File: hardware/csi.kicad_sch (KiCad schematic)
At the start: 1 part, among them J5 Conn_01x22_Female

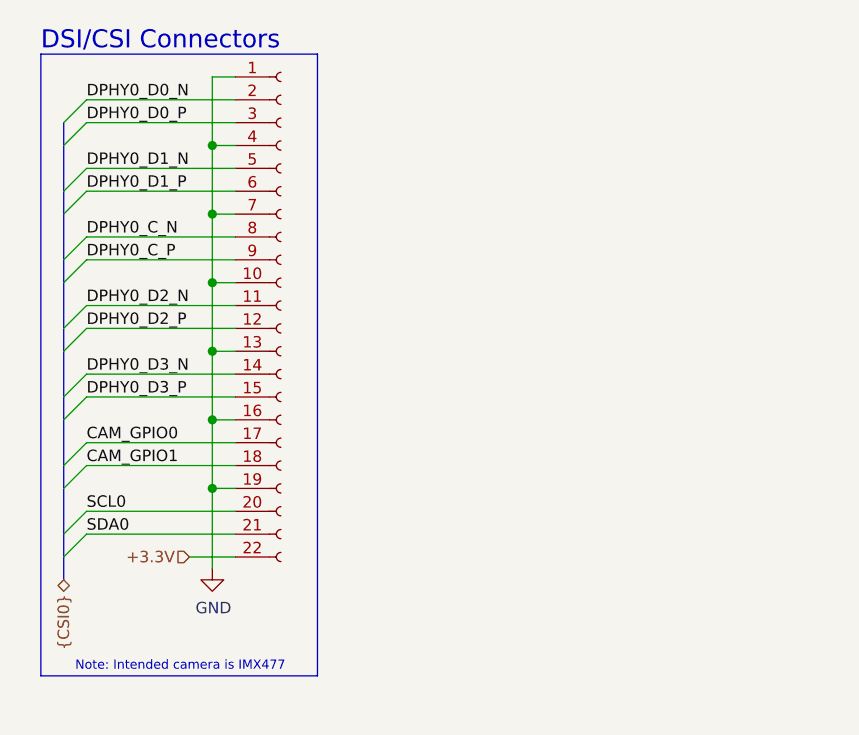
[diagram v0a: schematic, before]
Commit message: Add second camera, magnet load switch and schematic fixes
- Second camera J11 on MIPI1: I2C on ID_SD/ID_SC with 2.2k pull-ups,
  power enable on GPIO14/15 (CAM1_GPIO0/1); both cameras take 3.3 V
  from CM5_3.3V
- Magnet power switch: IC9 output is now +5V_AON, TPS22965 load switch
  IC15 drives +5V, J12 carries +5V_AON / MAG_ON / GND with R29
  pull-down; new TPS22965 symbol library
- Power: 4 A TPSM53604, 8 mOhm input sense resistor, C39/C40 bulk caps,
  F1-F3 battery polyfuses; 5 V raised to 5.115 V (R24 2.43k, 0.5 %
  feedback resistors); 47 uF at the CM5 5 V pins
- BMI270 on SPI and WSEN-PADS on I2C in serial_peripherals.kicad_sch
- Breakout headers J9/J13 with 5 V, 3.3 V and GND
- References renamed U -> IC; net classes for DPHY1, +5V, +5V_AON, +3.3V
- ERC clean (0 errors, 0 warnings); PCB update from the schematic is
  still in progress

Co-Authored-By: Claude Opus 5.5 <noreply@anthropic.com>
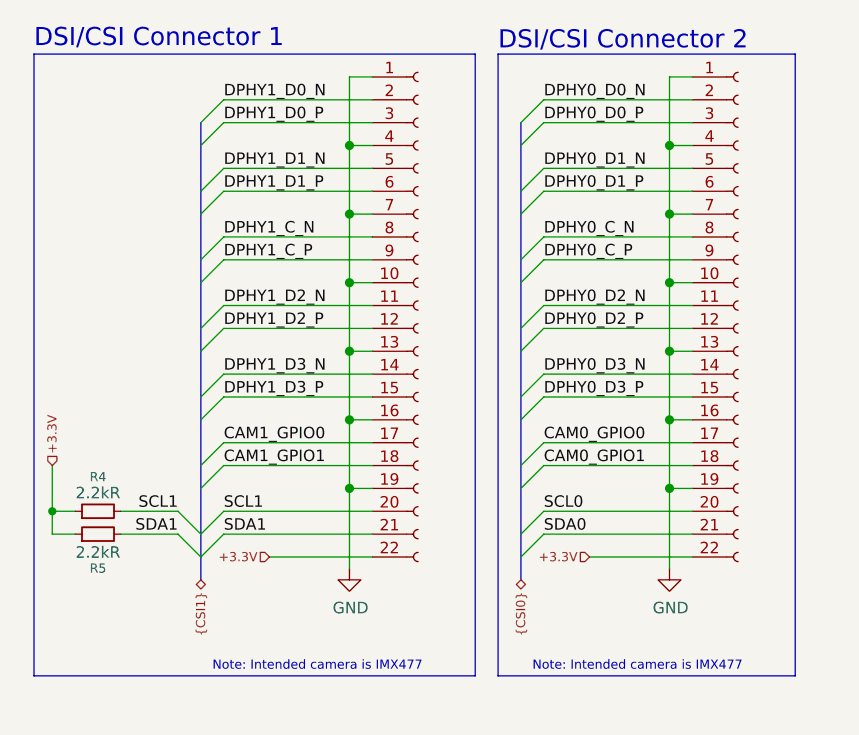
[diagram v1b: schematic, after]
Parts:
- added J11: Conn_01x22_Female, CM5IO:Hirose_FH12-22S-0.5SH_1x22-1MP_P0.50mm_Horizontal, symbol Connector:Conn_01x22_Socket
- added R4, R5: 2.2kR, Resistor_SMD:R_0402_1005Metric, symbol Device:R_Small
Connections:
- net +3.3V: now also J11.22 (Pin_22), R4.1, R5.1
- net GND: now also J11.1 (Pin_1), J11.10 (Pin_10), J11.13 (Pin_13), J11.16 (Pin_16), J11.19 (Pin_19), J11.4 (Pin_4), J11.7 (Pin_7)
- net CAM_GPIO0 renamed CAM0_GPIO0
- net CAM_GPIO1 renamed CAM0_GPIO1
- new net CAM1_GPIO0: J11.17 (Pin_17)
- new net CAM1_GPIO1: J11.18 (Pin_18)
- new net DPHY1_C_N: J11.8 (Pin_8)
- new net DPHY1_C_P: J11.9 (Pin_9)
- new net DPHY1_D0_N: J11.2 (Pin_2)
- new net DPHY1_D0_P: J11.3 (Pin_3)
- new net DPHY1_D1_N: J11.5 (Pin_5)
- new net DPHY1_D1_P: J11.6 (Pin_6)
- new net DPHY1_D2_N: J11.11 (Pin_11)
- new net DPHY1_D2_P: J11.12 (Pin_12)
- new net DPHY1_D3_N: J11.14 (Pin_14)
- new net DPHY1_D3_P: J11.15 (Pin_15)
- new net SCL1: J11.20 (Pin_20), R4.2
- new net SDA1: J11.21 (Pin_21), R5.2
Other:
- note added: "DSI/CSI Connector 1"
- note added: "DSI/CSI Connector 2"
- note removed: "DSI/CSI Connectors"

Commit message: Add switchable ESC power, vertical camera connectors and 3.3 V decoupling
- ESC power switch on the root sheet:
  - Battery input J6 changes to XT60PW-M. New XT60PW-F J14 carries switched
    power to both ESCs.
  - Q3 (onsemi NTMFS5C404NLT1G, 40 V, 0.67 mOhm) is driven by the photovoltaic
    driver IC16 (Vishay VOM1271T) from RP2354A GPIO14 (ESC_PWR_EN) via R31.
  - Soft start C46/D6/R32 keeps Q3 in its SOA while the ESC capacitors charge.
    D7 clamps the gate when the battery is unplugged or the thrusters windmill.
  - Static switch with no current limit: the battery BMS protects. Firmware
    timing rules are in the schematic note and the README.
- Camera connectors J5/J11 are now Molex 501951-2230 (vertical, flip lock).
  The footprint numbers pads n = Molex circuit 23-n so a standard Pi 22-pin
  cable lands GND on pin 1, as on the CM5 IO Board.
- Decoupling: 10 uF + 100 nF at the CM5 3.3 V output, 10 uF at each camera
  supply pin.
- Polyfuses F1-F3 removed; the battery feeds the charger path directly.
- New libraries VOM1271T, NTMFS5C404NL, Molex and Vishay, with 3D models.
- PCB updated from the schematic. The layout will be redone.

Co-Authored-By: Claude Opus 5.5 <noreply@anthropic.com>
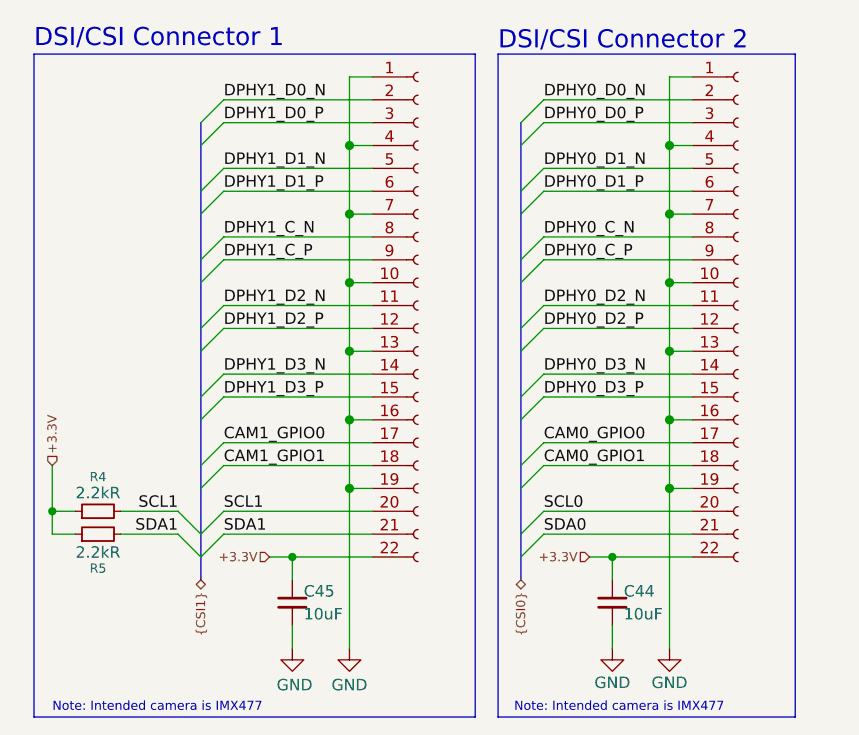
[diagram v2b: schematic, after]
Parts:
- added C44, C45: 10uF, Capacitor_SMD:C_0603_1608Metric, symbol Device:C_Small
- J11, J5: footprint CM5IO:Hirose_FH12-22S-0.5SH_1x22-1MP_P0.50mm_Horizontal -> Molex:Molex_501951-2230_1x22-1MP_P0.50mm_Vertical_RPi-CSI; MPN FH12-22S-0.5SH(55) -> 501951-2230; Manufacturer Hirose -> Molex; Mouser https://www.mouser.com/ProductDetail/798-FH12-22S-0.5SH55 -> https://mou.sr/4yP59iO; Mouser PN 798-FH12-22S-0.5SH55 -> 538-501951-2230
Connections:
- net +3.3V: now also C44.1, C45.1
- net GND: now also C44.2, C45.2

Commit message: Add LCSC part numbers and links, fix J7 part number
- Every part found on LCSC gets an "LCSC PN" (C-number) and an "LCSC" product
  link field, in the schematic and on the PCB footprints. Exact matches where
  LCSC lists the part; equivalents with the same specs where it does not or
  has no stock (C46, C26/C28/C30/C33/C34/C40, C29, C31, R6/R7, R21, R24,
  J3/J4, J7/J9/J13). Left empty: IC3, IC5 (not on LCSC), IC10, IC12
  (JLCPCB-only listings).
- J7: the MPN 61301421121 is a 2.54 mm header, but the footprint is 1.27 mm.
  Now Wurth 62201421121 (WR-PHD 1.27 mm 2x7) with matching description,
  datasheet and Mouser fields.
- Interactive HTML BOM in hardware/bom; KiCad project file re-saved.

Co-Authored-By: Claude Opus 5.5 <noreply@anthropic.com>
Claude-Session: https://claude.ai/code/session_01AhLYztcZikG9g81njGtEr1
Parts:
- C44, C45: LCSC (none) -> https://www.lcsc.com/product-detail/C19702.html; LCSC PN (none) -> C19702
- J11, J5: LCSC (none) -> https://www.lcsc.com/product-detail/C6819364.html; LCSC PN (none) -> C6819364
- R4, R5: LCSC (none) -> https://www.lcsc.com/product-detail/C114762.html; LCSC PN (none) -> C114762
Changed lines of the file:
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@@
+			)
+		)
+		(property "LCSC PN" "C6819364"
+			(at 57.15 45.72 0)
+			(hide yes)
+			(show_name no)
+			(do_not_autoplace no)
+			(effects
+				(font
+					(size 1.27 1.27)
+				)
+			)
+		)
+		(property "LCSC" "https://www.lcsc.com/product-detail/C6819364.html"
+			(at 57.15 45.72 0)
+			(hide yes)
+			(show_name no)
+			(do_not_autoplace no)
+			(effects
+				(font
+					(size 1.27 1.27)
+				)
 			)
 		)
@@
 			)
 		)
+		(property "LCSC PN" "C19702"
+			(at 78.74 78.74 0)
+			(hide yes)
+			(show_name no)
+			(do_not_autoplace no)
+			(effects
+				(font
+					(size 1.27 1.27)
+				)
+			)
+		)
+		(property "LCSC" "https://www.lcsc.com/product-detail/C19702.html"
+			(at 78.74 78.74 0)
+			(hide yes)
+			(show_name no)
+			(do_not_autoplace no)
+			(effects
+				(font
+					(size 1.27 1.27)
+				)
+			)
+		)
 		(pin "1"
 		)
@@
 			)
 		)
+		(property "LCSC PN" "C114762"
+			(at 21.59 71.12 0)
+			(hide yes)
+			(show_name no)
+			(do_not_autoplace no)
+			(effects
+				(font
+					(size 1.27 1.27)
+				)
+			)
+		)
+		(property "LCSC" "https://www.lcsc.com/product-detail/C114762.html"
+			(at 21.59 71.12 0)
+			(hide yes)
+			(show_name no)
+			(do_not_autoplace no)
+			(effects
+				(font
+					(size 1.27 1.27)
+				)
+			)
+		)
 		(pin "2"
 		)
@@
 			)
 		)
+		(property "LCSC PN" "C6819364"
+			(at 92.71 45.72 0)
+			(hide yes)
+			(show_name no)
+			(do_not_autoplace no)
+			(effects
+				(font
+					(size 1.27 1.27)
+				)
+			)
+		)
+		(property "LCSC" "https://www.lcsc.com/product-detail/C6819364.html"
+			(at 92.71 45.72 0)
+			(hide yes)
+			(show_name no)
+			(do_not_autoplace no)
+			(effects
+				(font
+					(size 1.27 1.27)
+				)
+			)
+		)
 		(pin "1"
 		)
@@
 			)
 		)
+		(property "LCSC PN" "C114762"
+			(at 21.59 68.58 0)
+			(hide yes)
+			(show_name no)
+			(do_not_autoplace no)
+			(effects
+				(font
+					(size 1.27 1.27)
+				)
+			)
+		)
+		(property "LCSC" "https://www.lcsc.com/product-detail/C114762.html"
+			(at 21.59 68.58 0)
+			(hide yes)
+			(show_name no)
+			(do_not_autoplace no)
+			(effects
+				(font
+					(size 1.27 1.27)
+				)
+			)
+		)
 		(pin "2"
 		)
@@
 			(at 43.18 78.74 0)
 			(hide yes)
+			(show_name no)
+			(do_not_autoplace no)
+			(effects
+				(font
+					(size 1.27 1.27)
+				)
+			)
+		)
+		(property "LCSC PN" "C19702"
+			(at 43.18 78.74 0)
+			(hide yes)
+			(show_name no)
+			(do_not_autoplace no)
+			(effects
+				(font
+					(size 1.27 1.27)
+				)
+			)
+		)
+		(property "LCSC" "https://www.lcsc.com/product-detail/C19702.html"
+			(at 43.18 78.74 0)
+			(hide yes)
